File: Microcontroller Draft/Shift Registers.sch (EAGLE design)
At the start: 13 parts, among them T317 BSS110, T7805 BSS110

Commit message: Started working in the output logic
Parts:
- removed T317, T7805, TLD33V: BSS110, transistor-fet:BSS110
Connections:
- removed net N$1: SR_INPUTA.QH, TLD33V.G
- removed net N$12: SR_INPUTA.QG, T7805.G
- removed net N$13: SR_INPUTA.QF, T317.G
- new net T_3V3: SR_INPUTA.QH
- new net T_5V: SR_INPUTA.QG
- new net T_VARV: SR_INPUTA.QF
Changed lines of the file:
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@@
 <part name="GND2" library="supply1" deviceset="GNDA" device=""/>
 <part name="+3V1" library="supply1" deviceset="+3V3" device=""/>
-<part name="T317" library="transistor-fet" deviceset="BSS110" device=""/>
-<part name="T7805" library="transistor-fet" deviceset="BSS110" device=""/>
-<part name="TLD33V" library="transistor-fet" deviceset="BSS110" device=""/>
 </parts>
 <sheets>
@@
 <instance part="GND2" gate="1" x="35.56" y="86.36"/>
 <instance part="+3V1" gate="G$1" x="35.56" y="132.08"/>
-<instance part="T317" gate="G$1" x="149.86" y="78.74"/>
-<instance part="T7805" gate="G$1" x="149.86" y="66.04"/>
-<instance part="TLD33V" gate="G$1" x="149.86" y="50.8"/>
 </instances>
 <busses>
@@
 </segment>
 </net>
-<net name="N$12" class="0">
+<net name="T_5V" class="0">
 <segment>
 <pinref part="SR_INPUT" gate="A" pin="QG"/>
 <wire x1="71.12" y1="63.5" x2="71.12" y2="104.14" width="0.1524" layer="91"/>
 <wire x1="71.12" y1="104.14" x2="63.5" y2="104.14" width="0.1524" layer="91"/>
-<wire x1="71.12" y1="63.5" x2="144.78" y2="63.5" width="0.1524" layer="91"/>
-<pinref part="T7805" gate="G$1" pin="G"/>
+<wire x1="71.12" y1="63.5" x2="165.1" y2="63.5" width="0.1524" layer="91"/>
+<label x="162.56" y="60.96" size="1.778" layer="95"/>
 </segment>
 </net>
-<net name="N$13" class="0">
+<net name="T_VARV" class="0">
 <segment>
 <pinref part="SR_INPUT" gate="A" pin="QF"/>
 <wire x1="73.66" y1="76.2" x2="73.66" y2="106.68" width="0.1524" layer="91"/>
 <wire x1="73.66" y1="106.68" x2="63.5" y2="106.68" width="0.1524" layer="91"/>
-<wire x1="73.66" y1="76.2" x2="144.78" y2="76.2" width="0.1524" layer="91"/>
-<pinref part="T317" gate="G$1" pin="G"/>
+<wire x1="73.66" y1="76.2" x2="165.1" y2="76.2" width="0.1524" layer="91"/>
+<label x="162.56" y="73.66" size="1.778" layer="95"/>
 </segment>
 </net>
@@
 </segment>
 </net>
-<net name="N$1" class="0">
+<net name="T_3V3" class="0">
 <segment>
 <pinref part="SR_INPUT" gate="A" pin="QH"/>
 <wire x1="63.5" y1="101.6" x2="68.58" y2="101.6" width="0.1524" layer="91"/>
 <wire x1="68.58" y1="101.6" x2="68.58" y2="48.26" width="0.1524" layer="91"/>
-<wire x1="68.58" y1="48.26" x2="144.78" y2="48.26" width="0.1524" layer="91"/>
-<pinref part="TLD33V" gate="G$1" pin="G"/>
+<wire x1="68.58" y1="48.26" x2="165.1" y2="48.26" width="0.1524" layer="91"/>
+<label x="162.56" y="45.72" size="1.778" layer="95"/>
 </segment>
 </net>

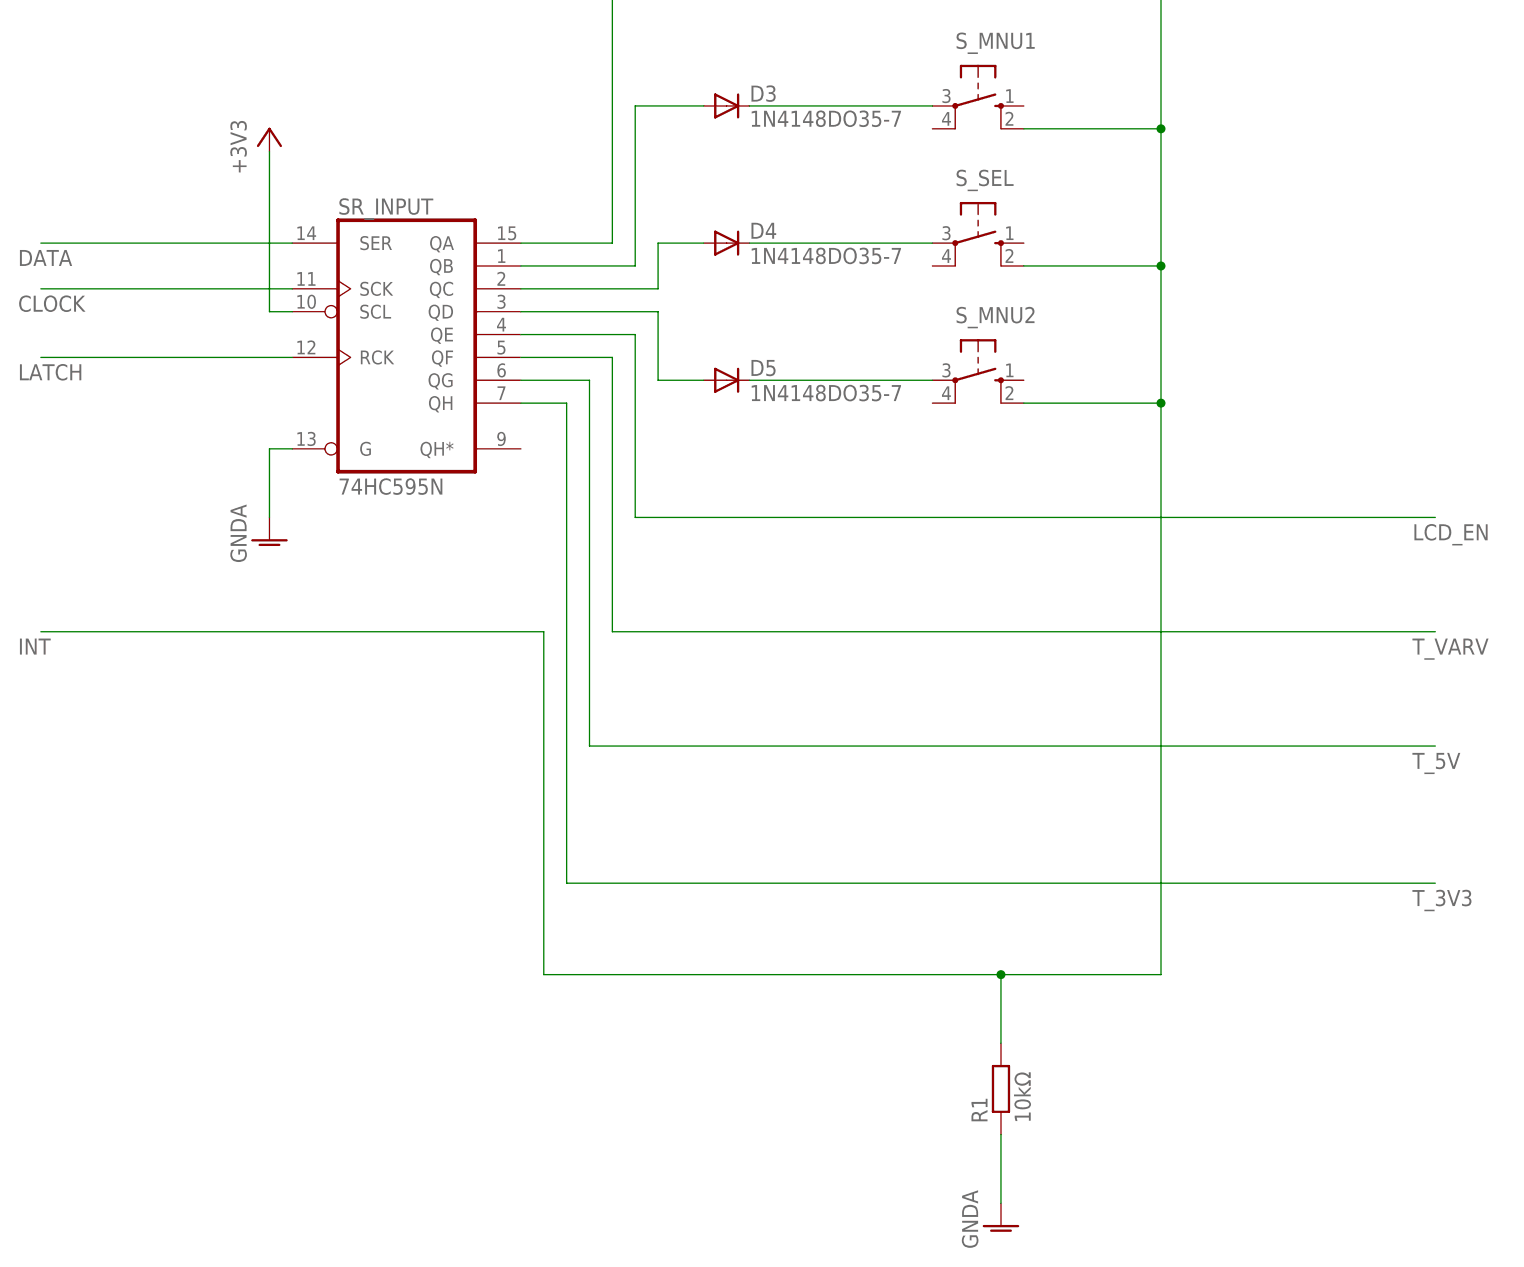
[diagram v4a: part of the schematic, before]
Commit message: Removed a button
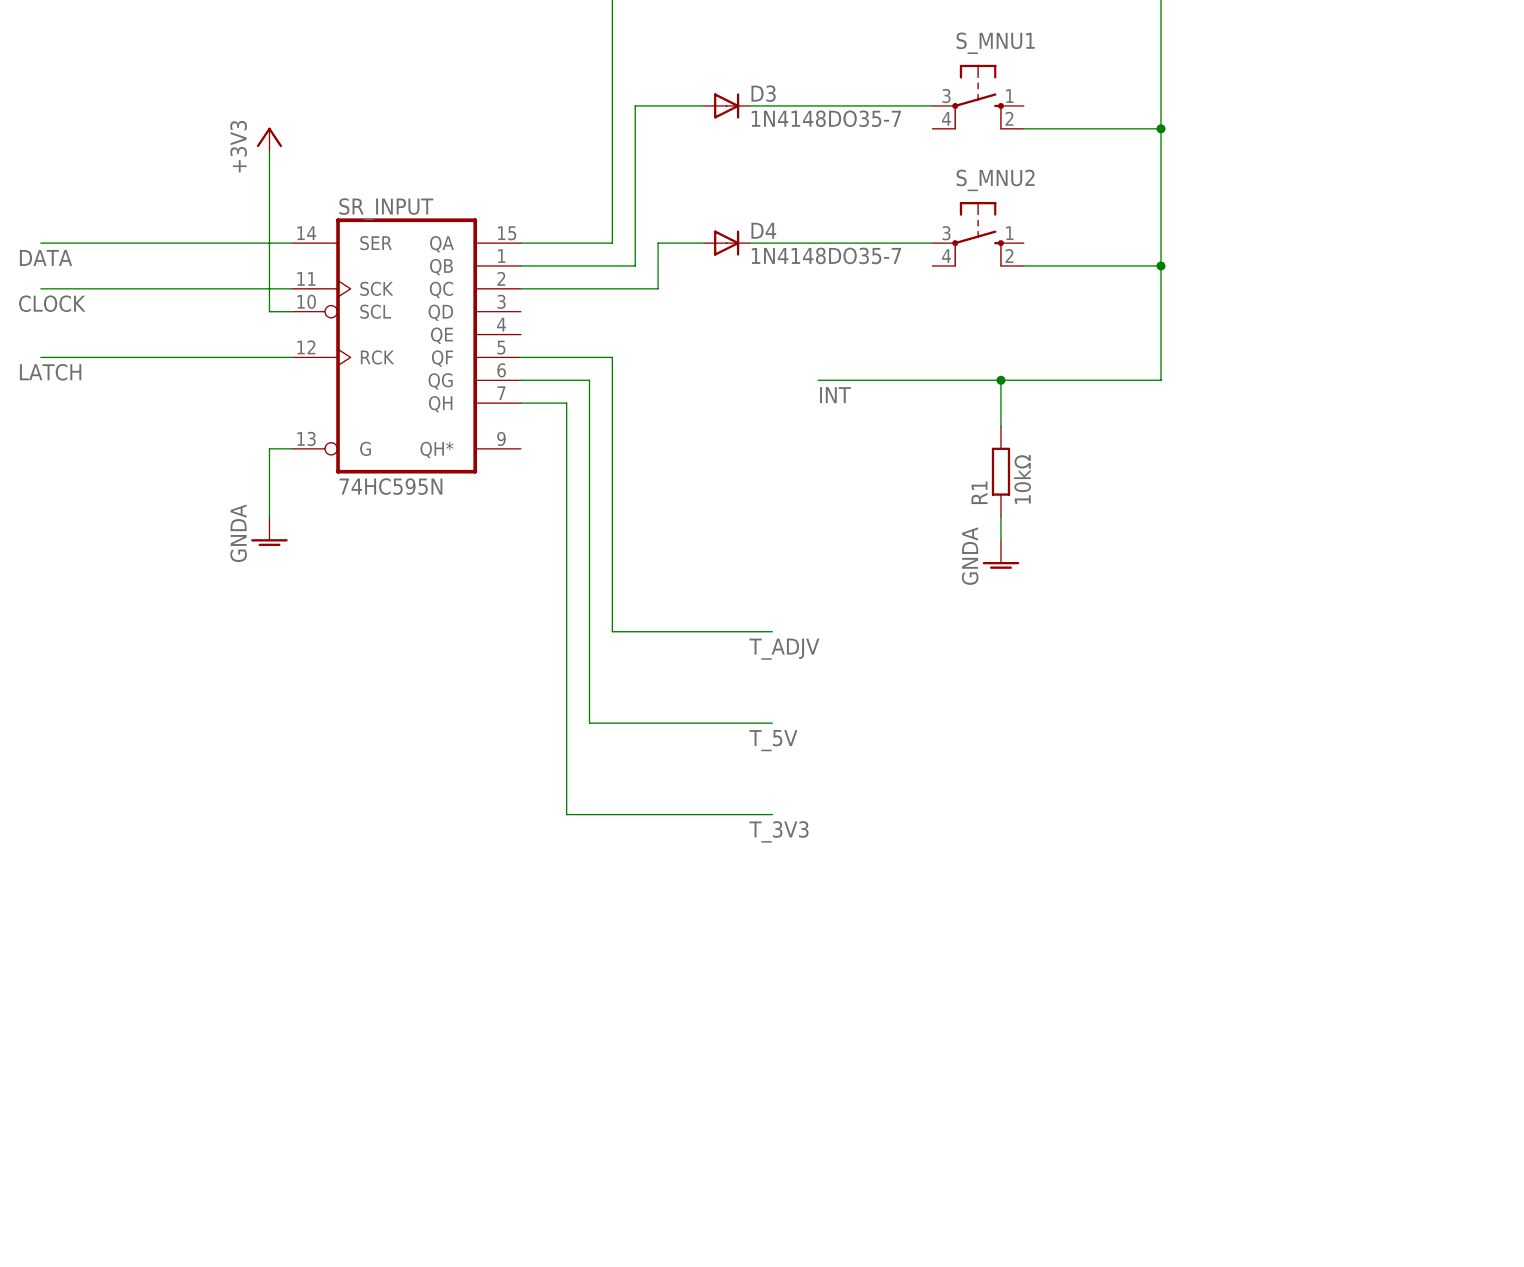
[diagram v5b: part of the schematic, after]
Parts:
- removed D5: 1N4148DO35-7, diode:1N4148DO35-7
- removed S_SEL: (no value), switch-omron:10-XX
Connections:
- net T_VARV renamed T_ADJV
- removed net LCD_EN: SR_INPUTA.QE
- removed net N$15: D5.A, SR_INPUTA.QD
- removed net N$5: D5.C, S_MNU2.P
- net INT: no longer S_SEL.S1
- net N$4: now also S_MNU2.P; no longer S_SEL.P
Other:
- moved on the sheet: R1, S_MNU2
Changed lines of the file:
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@@
 <part name="S_PWR" library="switch-omron" deviceset="10-XX" device=""/>
 <part name="S_MNU1" library="switch-omron" deviceset="10-XX" device=""/>
-<part name="S_SEL" library="switch-omron" deviceset="10-XX" device=""/>
 <part name="S_MNU2" library="switch-omron" deviceset="10-XX" device=""/>
 <part name="SR_INPUT" library="74xx-eu" deviceset="74*595" device="N" technology="HC"/>
@@
 <part name="D3" library="diode" deviceset="1N4148" device="DO35-7"/>
 <part name="D4" library="diode" deviceset="1N4148" device="DO35-7"/>
-<part name="D5" library="diode" deviceset="1N4148" device="DO35-7"/>
 <part name="GND2" library="supply1" deviceset="GNDA" device=""/>
 <part name="+3V1" library="supply1" deviceset="+3V3" device=""/>
@@
 <instance part="S_PWR" gate="1" x="114.3" y="160.02" rot="R270"/>
 <instance part="S_MNU1" gate="1" x="114.3" y="134.62" rot="R270"/>
-<instance part="S_SEL" gate="1" x="114.3" y="119.38" rot="R270"/>
-<instance part="S_MNU2" gate="1" x="114.3" y="104.14" rot="R270"/>
+<instance part="S_MNU2" gate="1" x="114.3" y="119.38" rot="R270"/>
 <instance part="SR_INPUT" gate="A" x="50.8" y="109.22"/>
-<instance part="R1" gate="G$1" x="116.84" y="25.4" rot="R90"/>
-<instance part="GND1" gate="1" x="116.84" y="10.16"/>
+<instance part="R1" gate="G$1" x="116.84" y="93.98" rot="R90"/>
+<instance part="GND1" gate="1" x="116.84" y="83.82"/>
 <instance part="D2" gate="G$1" x="86.36" y="160.02"/>
 <instance part="D3" gate="G$1" x="86.36" y="134.62"/>
 <instance part="D4" gate="G$1" x="86.36" y="119.38"/>
-<instance part="D5" gate="G$1" x="86.36" y="104.14"/>
 <instance part="GND2" gate="1" x="35.56" y="86.36"/>
 <instance part="+3V1" gate="G$1" x="35.56" y="132.08"/>
@@
 <wire x1="134.62" y1="157.48" x2="134.62" y2="132.08" width="0.1524" layer="91"/>
 <wire x1="134.62" y1="132.08" x2="134.62" y2="116.84" width="0.1524" layer="91"/>
-<wire x1="134.62" y1="116.84" x2="134.62" y2="101.6" width="0.1524" layer="91"/>
-<wire x1="134.62" y1="101.6" x2="134.62" y2="38.1" width="0.1524" layer="91"/>
-<wire x1="134.62" y1="38.1" x2="116.84" y2="38.1" width="0.1524" layer="91"/>
+<wire x1="134.62" y1="116.84" x2="134.62" y2="104.14" width="0.1524" layer="91"/>
+<wire x1="134.62" y1="104.14" x2="116.84" y2="104.14" width="0.1524" layer="91"/>
 <pinref part="S_MNU1" gate="1" pin="S1"/>
-<wire x1="116.84" y1="38.1" x2="66.04" y2="38.1" width="0.1524" layer="91"/>
 <wire x1="119.38" y1="132.08" x2="134.62" y2="132.08" width="0.1524" layer="91"/>
-<pinref part="S_SEL" gate="1" pin="S1"/>
+<pinref part="S_MNU2" gate="1" pin="S1"/>
 <wire x1="119.38" y1="116.84" x2="134.62" y2="116.84" width="0.1524" layer="91"/>
-<pinref part="S_MNU2" gate="1" pin="S1"/>
-<wire x1="119.38" y1="101.6" x2="134.62" y2="101.6" width="0.1524" layer="91"/>
 <junction x="134.62" y="132.08"/>
 <junction x="134.62" y="116.84"/>
-<junction x="134.62" y="101.6"/>
 <pinref part="R1" gate="G$1" pin="2"/>
-<wire x1="116.84" y1="30.48" x2="116.84" y2="38.1" width="0.1524" layer="91"/>
-<junction x="116.84" y="38.1"/>
-<wire x1="10.16" y1="76.2" x2="66.04" y2="76.2" width="0.1524" layer="91"/>
-<wire x1="66.04" y1="76.2" x2="66.04" y2="38.1" width="0.1524" layer="91"/>
-<label x="7.62" y="73.66" size="1.778" layer="95"/>
+<wire x1="116.84" y1="99.06" x2="116.84" y2="104.14" width="0.1524" layer="91"/>
+<wire x1="116.84" y1="104.14" x2="96.52" y2="104.14" width="0.1524" layer="91"/>
+<label x="96.52" y="101.6" size="1.778" layer="95"/>
+<junction x="116.84" y="104.14"/>
 </segment>
 </net>
@@
 <pinref part="GND1" gate="1" pin="GNDA"/>
 <pinref part="R1" gate="G$1" pin="1"/>
-<wire x1="116.84" y1="12.7" x2="116.84" y2="20.32" width="0.1524" layer="91"/>
+<wire x1="116.84" y1="86.36" x2="116.84" y2="88.9" width="0.1524" layer="91"/>
 </segment>
 <segment>
@@
 <segment>
 <pinref part="D4" gate="G$1" pin="C"/>
-<pinref part="S_SEL" gate="1" pin="P"/>
+<pinref part="S_MNU2" gate="1" pin="P"/>
 <wire x1="88.9" y1="119.38" x2="109.22" y2="119.38" width="0.1524" layer="91"/>
-</segment>
-</net>
-<net name="N$5" class="0">
-<segment>
-<pinref part="D5" gate="G$1" pin="C"/>
-<pinref part="S_MNU2" gate="1" pin="P"/>
-<wire x1="88.9" y1="104.14" x2="109.22" y2="104.14" width="0.1524" layer="91"/>
 </segment>
 </net>
@@
 <segment>
 <pinref part="SR_INPUT" gate="A" pin="QG"/>
-<wire x1="71.12" y1="63.5" x2="71.12" y2="104.14" width="0.1524" layer="91"/>
+<wire x1="71.12" y1="66.04" x2="71.12" y2="104.14" width="0.1524" layer="91"/>
 <wire x1="71.12" y1="104.14" x2="63.5" y2="104.14" width="0.1524" layer="91"/>
-<wire x1="71.12" y1="63.5" x2="165.1" y2="63.5" width="0.1524" layer="91"/>
-<label x="162.56" y="60.96" size="1.778" layer="95"/>
+<wire x1="71.12" y1="66.04" x2="91.44" y2="66.04" width="0.1524" layer="91"/>
+<label x="88.9" y="63.5" size="1.778" layer="95"/>
 </segment>
 </net>
-<net name="T_VARV" class="0">
+<net name="T_ADJV" class="0">
 <segment>
 <pinref part="SR_INPUT" gate="A" pin="QF"/>
 <wire x1="73.66" y1="76.2" x2="73.66" y2="106.68" width="0.1524" layer="91"/>
 <wire x1="73.66" y1="106.68" x2="63.5" y2="106.68" width="0.1524" layer="91"/>
-<wire x1="73.66" y1="76.2" x2="165.1" y2="76.2" width="0.1524" layer="91"/>
-<label x="162.56" y="73.66" size="1.778" layer="95"/>
-</segment>
-</net>
-<net name="LCD_EN" class="0">
-<segment>
-<wire x1="165.1" y1="88.9" x2="76.2" y2="88.9" width="0.1524" layer="91"/>
-<wire x1="76.2" y1="88.9" x2="76.2" y2="109.22" width="0.1524" layer="91"/>
-<pinref part="SR_INPUT" gate="A" pin="QE"/>
-<wire x1="76.2" y1="109.22" x2="63.5" y2="109.22" width="0.1524" layer="91"/>
-<label x="162.56" y="86.36" size="1.778" layer="95"/>
-</segment>
-</net>
-<net name="N$15" class="0">
-<segment>
-<pinref part="D5" gate="G$1" pin="A"/>
-<wire x1="83.82" y1="104.14" x2="78.74" y2="104.14" width="0.1524" layer="91"/>
-<wire x1="78.74" y1="104.14" x2="78.74" y2="111.76" width="0.1524" layer="91"/>
-<pinref part="SR_INPUT" gate="A" pin="QD"/>
-<wire x1="78.74" y1="111.76" x2="63.5" y2="111.76" width="0.1524" layer="91"/>
+<wire x1="73.66" y1="76.2" x2="91.44" y2="76.2" width="0.1524" layer="91"/>
+<label x="88.9" y="73.66" size="1.778" layer="95"/>
 </segment>
 </net>
@@
 <pinref part="SR_INPUT" gate="A" pin="QH"/>
 <wire x1="63.5" y1="101.6" x2="68.58" y2="101.6" width="0.1524" layer="91"/>
-<wire x1="68.58" y1="101.6" x2="68.58" y2="48.26" width="0.1524" layer="91"/>
-<wire x1="68.58" y1="48.26" x2="165.1" y2="48.26" width="0.1524" layer="91"/>
-<label x="162.56" y="45.72" size="1.778" layer="95"/>
+<wire x1="68.58" y1="101.6" x2="68.58" y2="55.88" width="0.1524" layer="91"/>
+<wire x1="68.58" y1="55.88" x2="91.44" y2="55.88" width="0.1524" layer="91"/>
+<label x="88.9" y="53.34" size="1.778" layer="95"/>
 </segment>
 </net>
